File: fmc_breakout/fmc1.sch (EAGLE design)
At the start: 1 part

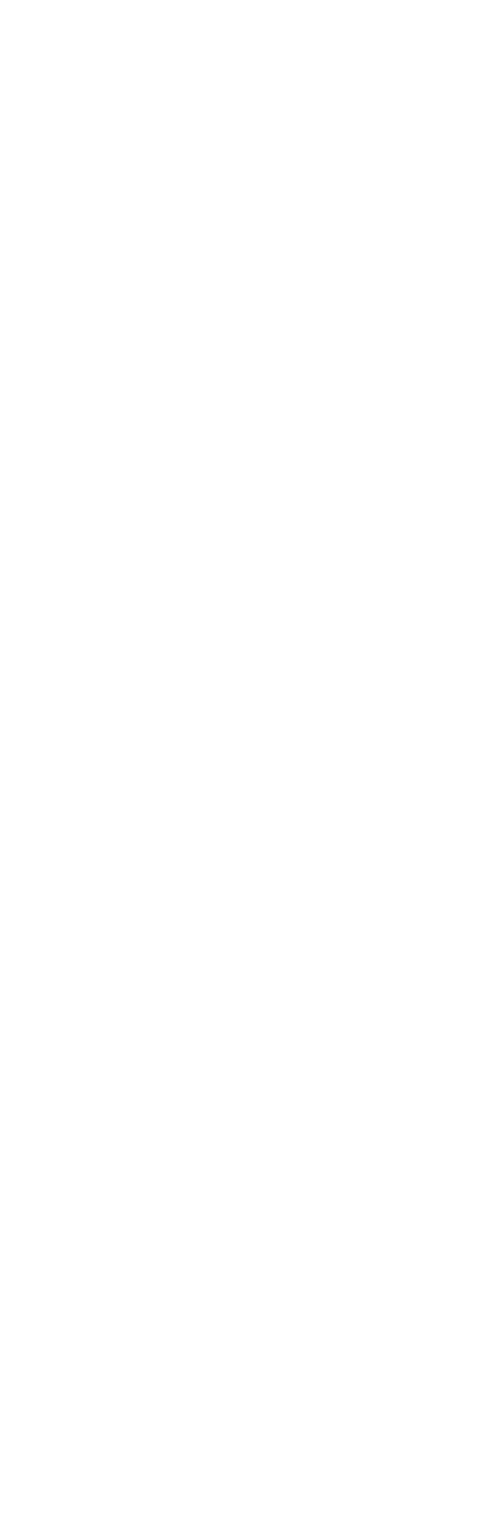
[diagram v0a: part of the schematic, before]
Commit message: fixed EAGLE problems, added FIFOs to FMC breakout
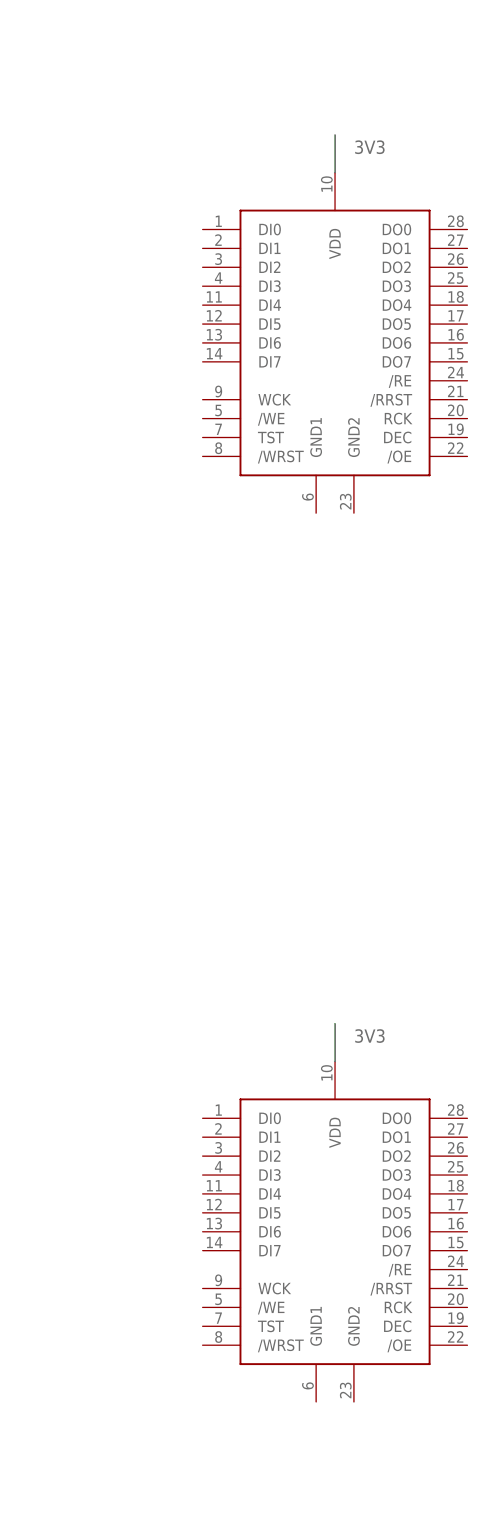
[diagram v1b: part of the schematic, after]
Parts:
- added AL422B, U$2: AL422B, AL422B:AL422B
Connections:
- net 3V3: now also AL422B.VDD, U$2.VDD
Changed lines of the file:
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@@
 <part name="ZED1" library="zed-board" deviceset="ZED-BOARD" device=""/>
 <part name="FRAME1" library="frames" deviceset="A3L-LOC" device="" value="ZED FMC breakout"/>
+<part name="AL422B" library="AL422B" deviceset="AL422B" device=""/>
+<part name="U$2" library="AL422B" deviceset="AL422B" device=""/>
 </parts>
 <sheets>
@@
 <instance part="ZED1" gate="-B" x="68.58" y="-55.88"/>
 <instance part="FRAME1" gate="G$1" x="-2.54" y="-121.92"/>
+<instance part="AL422B" gate="G$1" x="190.5" y="73.66"/>
+<instance part="U$2" gate="G$1" x="190.5" y="-45.72"/>
 </instances>
 <busses>
@@
 <label x="86.36" y="40.64" size="1.778" layer="95"/>
 </segment>
-</net>
+<segment>
+<pinref part="AL422B" gate="G$1" pin="VDD"/>
+<wire x1="190.5" y1="96.52" x2="190.5" y2="101.6" width="0.1524" layer="91"/>
+<label x="193.04" y="99.06" size="1.778" layer="95"/>
+</segment>
+<segment>
+<pinref part="U$2" gate="G$1" pin="VDD"/>
+<wire x1="190.5" y1="-22.86" x2="190.5" y2="-17.78" width="0.1524" layer="91"/>
+<label x="193.04" y="-20.32" size="1.778" layer="95"/>
+</segment>
+</net>

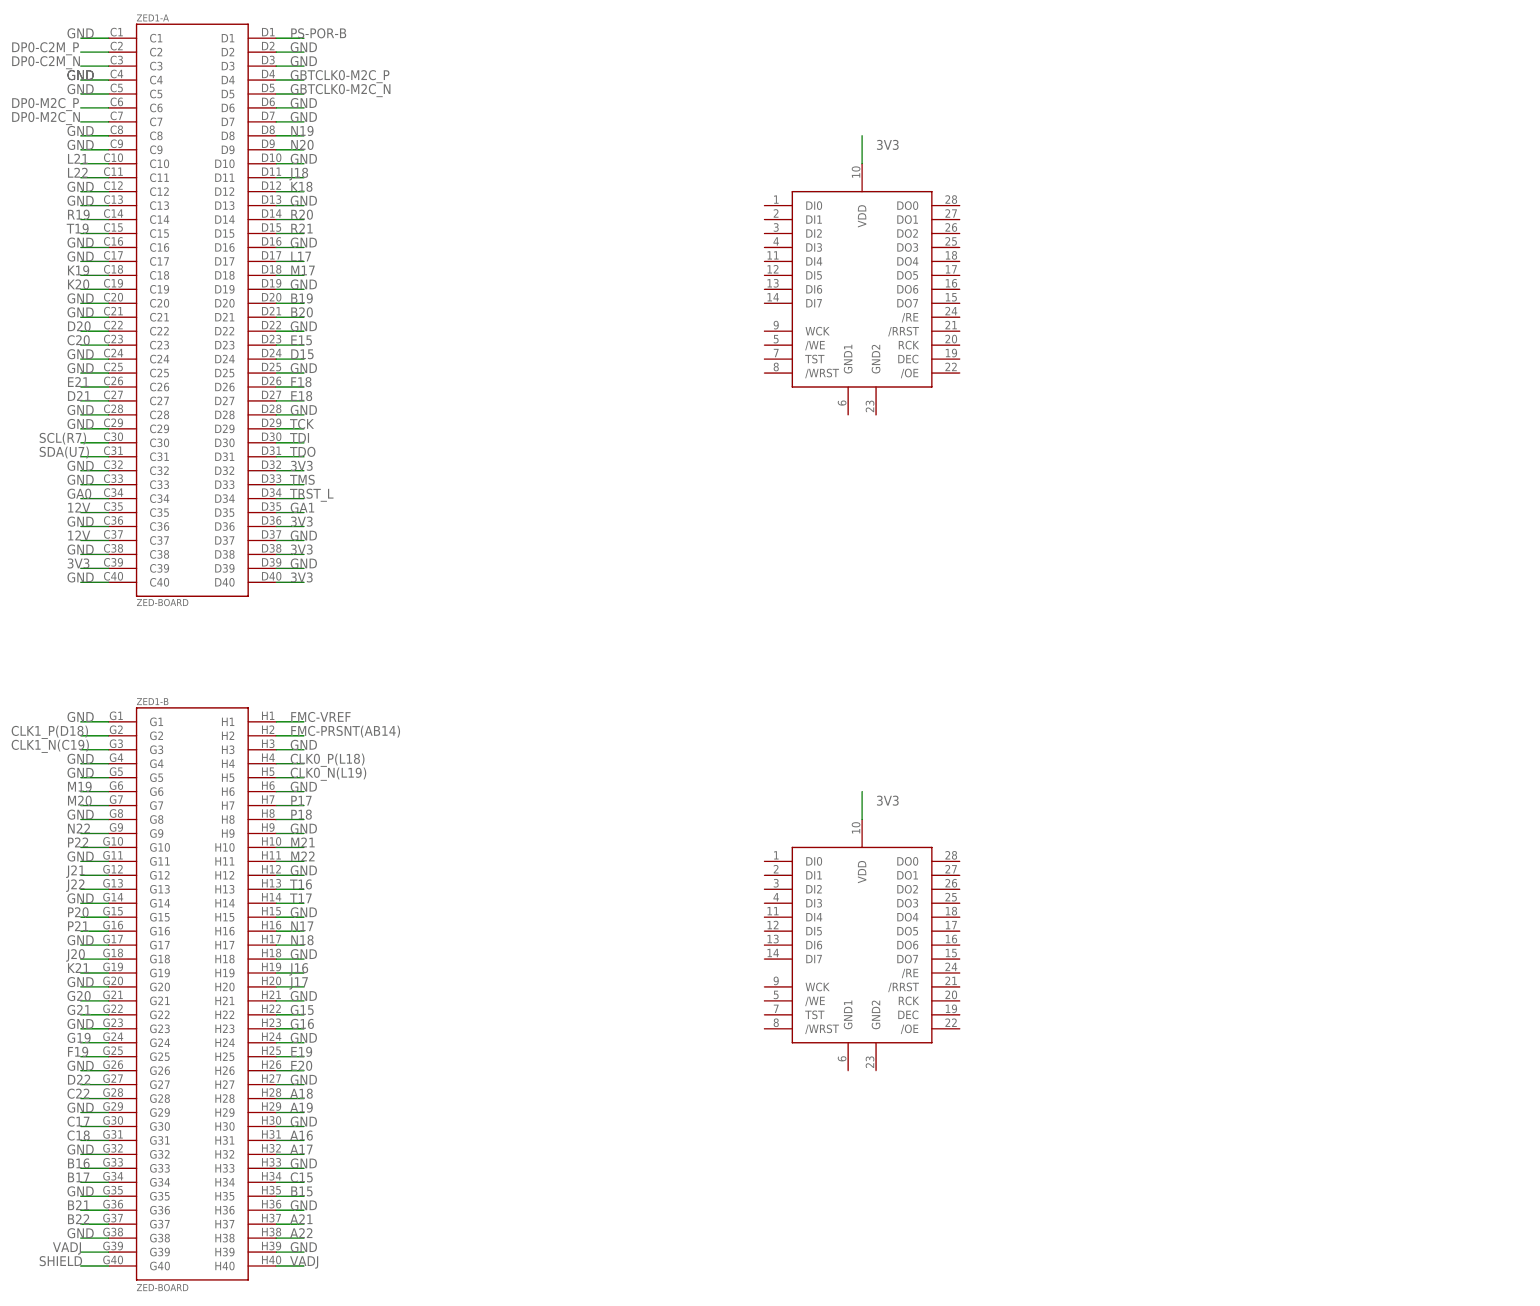
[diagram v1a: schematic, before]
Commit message: added camera data headers
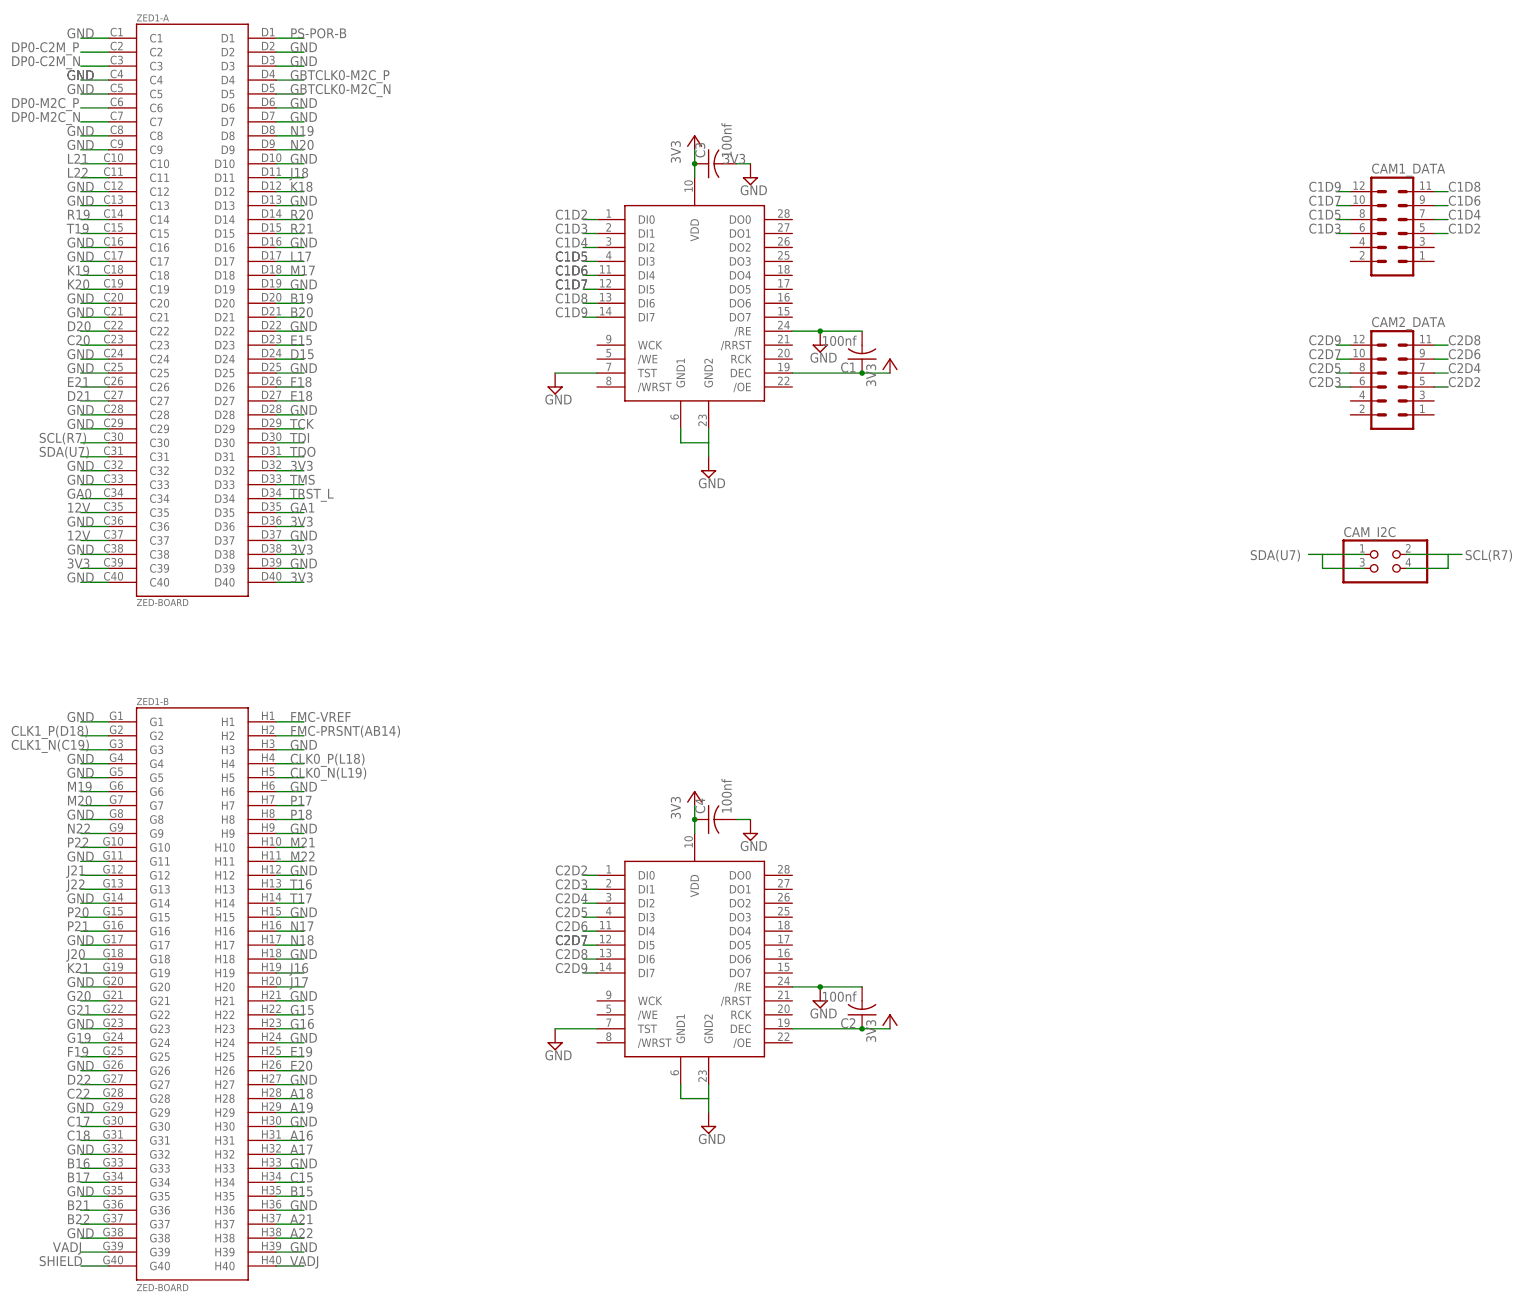
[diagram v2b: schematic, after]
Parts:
- added C1, C2, C3, C4: 100nf, rcl:C-US025-024X044
- added CAM1_DATA, CAM2_DATA: (no value), con-lstb:MA06-2
- added CAM_I2C: (no value), pinhead:PINHD-2X2
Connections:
- new net +3V3: AL422B.DEC, C1.1, C2.1, U$2.DEC
- new net C1D2: AL422B.DI0, CAM1_DATA.5
- new net C1D3: AL422B.DI1, CAM1_DATA.6
- new net C1D4: AL422B.DI2, CAM1_DATA.7
- new net C1D5: AL422B.DI3, CAM1_DATA.8
- new net C1D6: AL422B.DI4, CAM1_DATA.9
- new net C1D7: AL422B.DI5, CAM1_DATA.10
- new net C1D8: AL422B.DI6, CAM1_DATA.11
- new net C1D9: AL422B.DI7, CAM1_DATA.12
- new net C2D2: CAM2_DATA.5, U$2.DI0
- new net C2D3: CAM2_DATA.6, U$2.DI1
- new net C2D4: CAM2_DATA.7, U$2.DI2
- new net C2D5: CAM2_DATA.8, U$2.DI3
- new net C2D6: CAM2_DATA.9, U$2.DI4
- new net C2D7: CAM2_DATA.10, U$2.DI5
- new net C2D8: CAM2_DATA.11, U$2.DI6
- new net C2D9: CAM2_DATA.12, U$2.DI7
- net 3V3: now also C3.1, C4.1
- net GND: now also AL422B./RE, AL422B.GND1, AL422B.GND2, AL422B.TST, C1.2, C2.2, C3.2, C4.2, U$2./RE, U$2.GND1, U$2.GND2, U$2.TST
- net SCL(R7): now also CAM_I2C.2, CAM_I2C.4
- net SDA(U7): now also CAM_I2C.1, CAM_I2C.3
